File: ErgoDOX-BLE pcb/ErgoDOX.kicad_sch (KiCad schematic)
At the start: 98 parts, among them J1 Conn_01x04, J2 Conn_01x02_Female, J3 Conn_01x02_Female, J4 Conn_01x02, J5 Conn_01x02, P1 USB_C_Plug_USB2.0, Q1 Q_NPN_BCE, SW0:10 SW0:3, SW0:11 SW0:2, SW0:12 SW0:1, SW0:7 SW0:6, SW0:8 SW0:5, SW0:9 SW0:4, SW1:10 SW1:3, SW1:11 SW1:2, SW1:12 SW1:1, SW1:13 SW1:0, SW1:9 SW1:4, SW2:10 SW2:3, SW2:11 SW2:2, SW2:12 SW2:1, SW2:13 SW2:0, SW2:7 SW2:6, SW2:8 SW2:5, SW2:9 SW2:4, SW3:10 SW3:3, SW3:11 SW3:2, SW3:12 SW3:1, SW3:13 SW3:0, SW3:8 SW3:5, SW3:9 SW3:4, SW4:10 SW4:3, SW4:11 SW4:2, SW4:12 SW4:1, SW4:13 SW4:0, SW4:7 SW4:6, SW4:8 SW4:5, SW4:9 SW4:4, SW5:10 SW5:3, SW5:11 SW5:2, SW5:12 SW5:1, SW5:13 SW5:0, SW5:7 SW5:6, SW5:8 SW5:5, SW5:9 SW5:4, U1 MCP23018

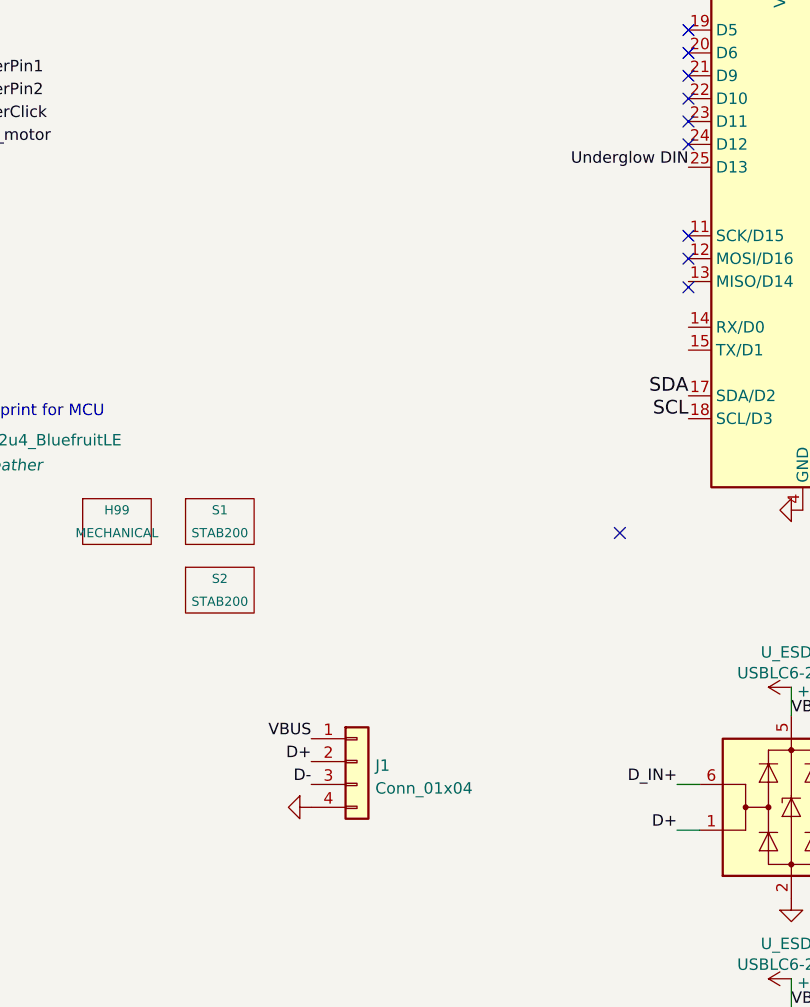
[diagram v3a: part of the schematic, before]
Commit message: Start adding audio port
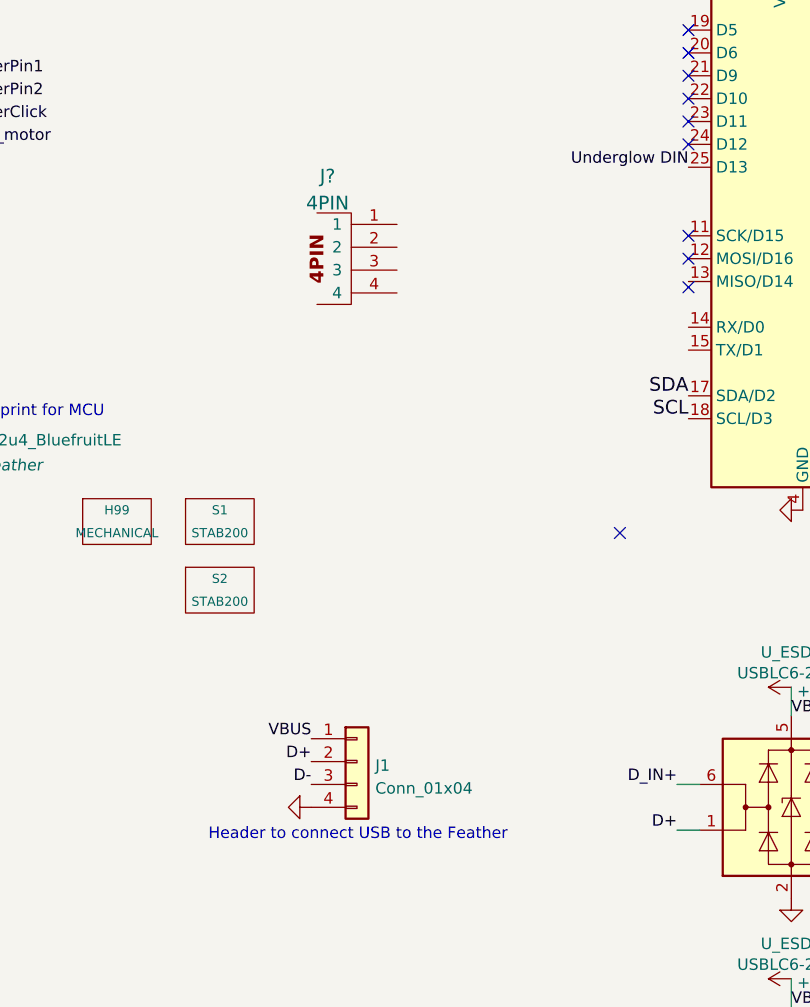
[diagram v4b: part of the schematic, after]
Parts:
- added J?: 4PIN, symbol component:4PIN
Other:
- note added: "Header to connect USB to the Feather"
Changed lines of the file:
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@@
     (effects (font (size 1.27 1.27)) (justify right bottom))
+  )
+  (text "Header to connect USB to the Feather" (at 187.96 148.59 0)
+    (effects (font (size 1.27 1.27)) (justify left bottom))
   )
   (text "Vibration motor circuit. Resistor should be 42 ohms or more"
@@
     )
     (pin "1")
+  )
+  (symbol (lib_id "component:4PIN") (at 203.835 83.82 0) (unit 1)
+    (in_bom yes) (on_board yes) (fields_autoplaced)
+    (property "Reference" "J?" (id 0) (at 201.2023 74.6559 0)
+      (effects (font (size 1.524 1.524)))
+    )
+    (property "Value" "4PIN" (id 1) (at 201.2023 77.6493 0)
+      (effects (font (size 1.524 1.524)))
+    )
+    (property "Footprint" "" (id 2) (at 203.835 83.82 0)
+      (effects (font (size 1.27 1.27)) hide)
+    )
+    (property "Datasheet" "" (id 3) (at 203.835 83.82 0)
+      (effects (font (size 1.27 1.27)) hide)
+    )
+    (pin "1")
+    (pin "2")
+    (pin "3")
+    (pin "4")
   )
   (symbol (lib_id "power:+5V") (at 207.645 216.535 0) (unit 1)
@@
       (reference "J5") (unit 1) (value "Conn_01x02") (footprint "Connector_PinHeader_2.00mm:PinHeader_1x02_P2.00mm_Vertical")
     )
+    (path "/e432a4c5-f3c6-4cf3-aa9d-4b1045904339"
+      (reference "J?") (unit 1) (value "4PIN") (footprint "")
+    )
     (path "/131c2f34-19ec-4ccc-8120-2b0363648606"

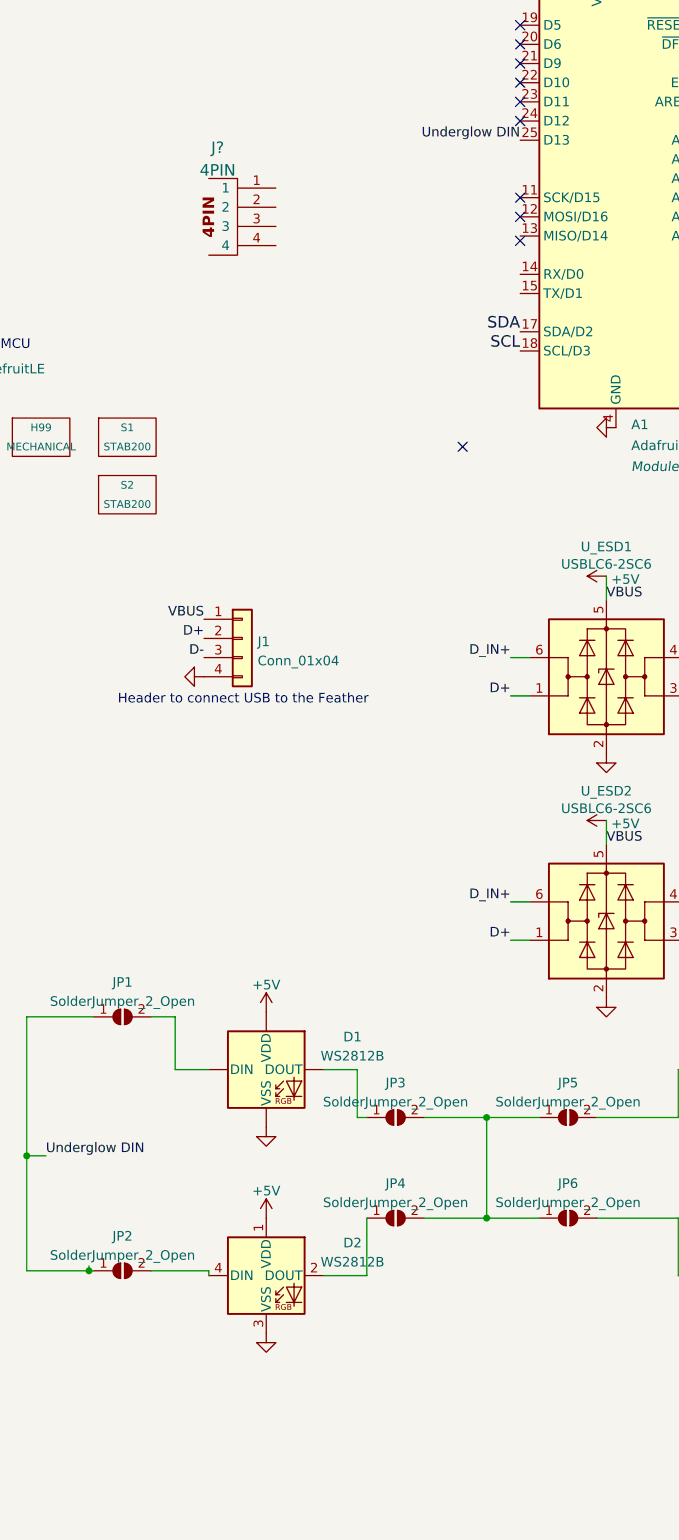
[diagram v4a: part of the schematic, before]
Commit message: Do initial placement of TRRS jack
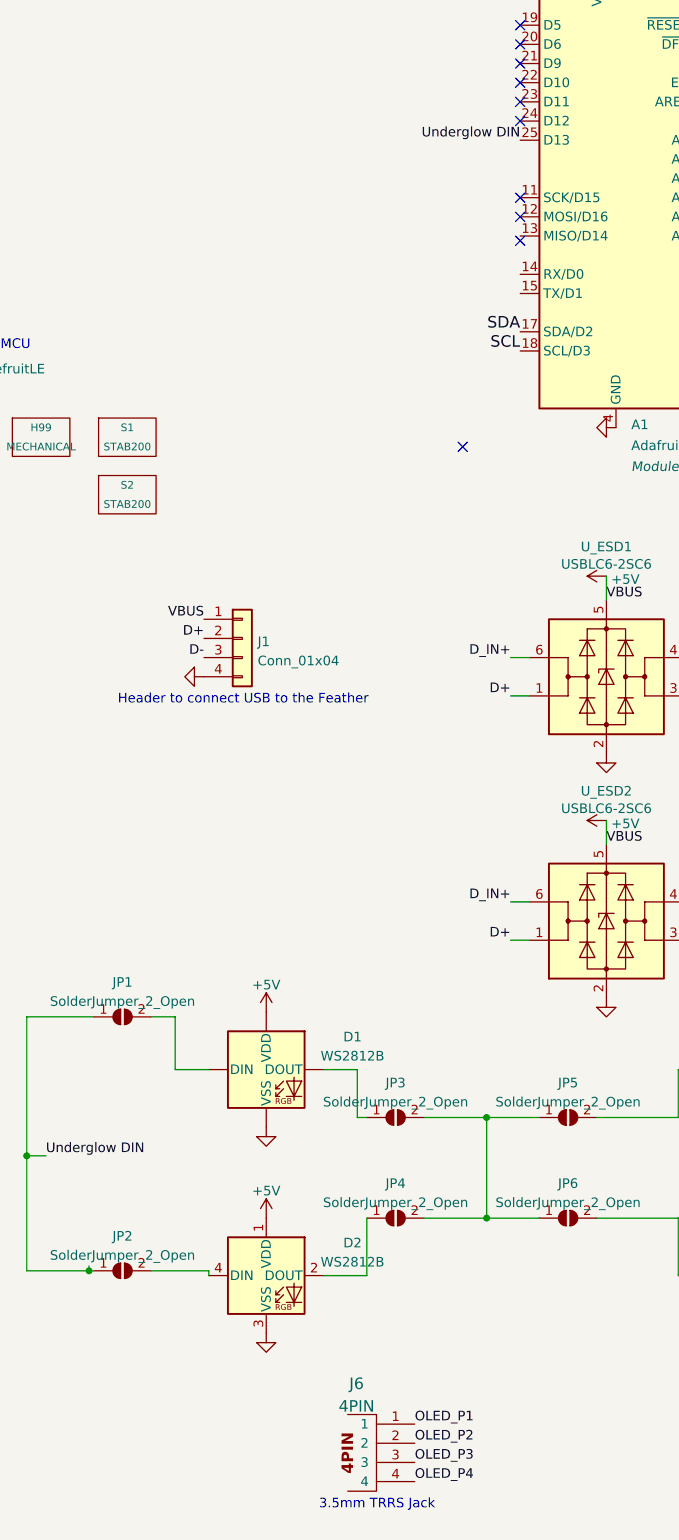
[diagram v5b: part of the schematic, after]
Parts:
- J6: renamed from J?; footprint (none) -> ErgoDOX pcb:4pin35mmAudio
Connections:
- net OLED_P1: now also J6.1
- net OLED_P2: now also J6.2
- net OLED_P3: now also J6.3
- net OLED_P4: now also J6.4
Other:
- note added: "3.5mm TRRS Jack"
- moved on the sheet: J6
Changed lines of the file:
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@@
+    (effects (font (size 1.27 1.27)) (justify left bottom))
+  )
+  (text "3.5mm TRRS Jack" (at 214.63 255.27 0)
     (effects (font (size 1.27 1.27)) (justify left bottom))
   )
@@
     (effects (font (size 1.524 1.524)) (justify left bottom))
   )
+  (label "OLED_P2" (at 227.33 246.38 0)
+    (effects (font (size 1.27 1.27)) (justify left bottom))
+  )
   (label "D+" (at 199.39 139.7 180)
     (effects (font (size 1.27 1.27)) (justify right bottom))
@@
     (effects (font (size 1.27 1.27)) (justify right bottom))
   )
+  (label "OLED_P1" (at 227.33 243.84 0)
+    (effects (font (size 1.27 1.27)) (justify left bottom))
+  )
   (label "ROW3" (at 340.36 85.09 0)
     (effects (font (size 1.524 1.524)) (justify left bottom))
@@
     (effects (font (size 1.524 1.524)) (justify left bottom))
   )
+  (label "OLED_P4" (at 227.33 251.46 0)
+    (effects (font (size 1.27 1.27)) (justify left bottom))
+  )
   (label "VBUS" (at 47.625 80.645 0)
     (effects (font (size 1.27 1.27)) (justify left bottom))
@@
   (label "Reset_SW" (at 58.42 25.4 180)
     (effects (font (size 1.27 1.27)) (justify right bottom))
+  )
+  (label "OLED_P3" (at 227.33 248.92 0)
+    (effects (font (size 1.27 1.27)) (justify left bottom))
   )
   (label "ROW4" (at 340.36 82.55 0)
@@
   (symbol (lib_id "power:+3V3") (at 297.815 188.595 0) (unit 1)
     (in_bom yes) (on_board yes) (fields_autoplaced)
-    (property "Reference" "#PWR?" (id 0) (at 297.815 192.405 0)
+    (property "Reference" "#PWR017" (id 0) (at 297.815 192.405 0)
       (effects (font (size 1.27 1.27)) hide)
     )
@@
     (pin "1")
   )
-  (symbol (lib_id "component:4PIN") (at 203.835 83.82 0) (unit 1)
-    (in_bom yes) (on_board yes) (fields_autoplaced)
-    (property "Reference" "J?" (id 0) (at 201.2023 74.6559 0)
+  (symbol (lib_id "component:4PIN") (at 222.25 247.65 0) (unit 1)
+    (in_bom yes) (on_board yes) (fields_autoplaced)
+    (property "Reference" "J6" (id 0) (at 219.6173 238.4859 0)
       (effects (font (size 1.524 1.524)))
     )
-    (property "Value" "4PIN" (id 1) (at 201.2023 77.6493 0)
+    (property "Value" "4PIN" (id 1) (at 219.6173 241.4793 0)
       (effects (font (size 1.524 1.524)))
     )
-    (property "Footprint" "" (id 2) (at 203.835 83.82 0)
-      (effects (font (size 1.27 1.27)) hide)
-    )
-    (property "Datasheet" "" (id 3) (at 203.835 83.82 0)
+    (property "Footprint" "ErgoDOX pcb:4pin35mmAudio" (id 2) (at 222.25 247.65 0)
+      (effects (font (size 1.27 1.27)) hide)
+    )
+    (property "Datasheet" "" (id 3) (at 222.25 247.65 0)
       (effects (font (size 1.27 1.27)) hide)
     )
@@
       (reference "#PWR016") (unit 1) (value "+5V") (footprint "")
     )
+    (path "/9262c7d3-8469-461f-b560-6292a46b6254"
+      (reference "#PWR017") (unit 1) (value "+3V3") (footprint "")
+    )
     (path "/b2ff08d7-b8f1-4672-b1f1-bb796fc3abc5"
       (reference "#PWR018") (unit 1) (value "GND") (footprint "")
@@
       (reference "#PWR0107") (unit 1) (value "+5V") (footprint "")
     )
-    (path "/9262c7d3-8469-461f-b560-6292a46b6254"
-      (reference "#PWR?") (unit 1) (value "+3V3") (footprint "")
-    )
     (path "/dc3e5149-0691-4e48-82aa-18a33c58d220"
       (reference "A1") (unit 1) (value "Adafruit_Feather_32u4_BluefruitLE") (footprint "Module:Adafruit_Feather")
@@
     )
     (path "/e432a4c5-f3c6-4cf3-aa9d-4b1045904339"
-      (reference "J?") (unit 1) (value "4PIN") (footprint "")
+      (reference "J6") (unit 1) (value "4PIN") (footprint "ErgoDOX pcb:4pin35mmAudio")
     )
     (path "/131c2f34-19ec-4ccc-8120-2b0363648606"

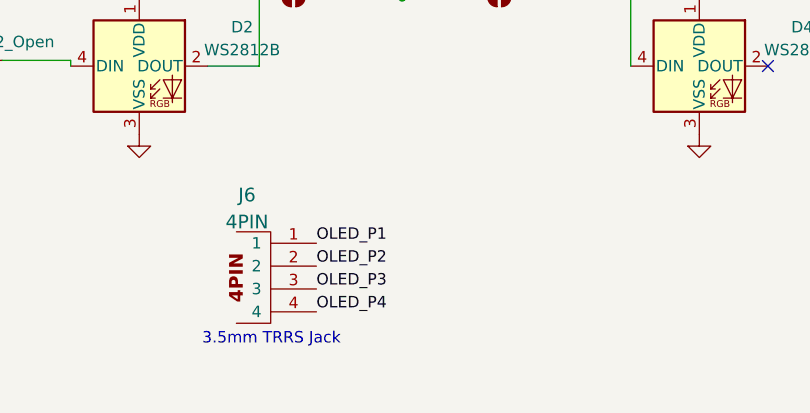
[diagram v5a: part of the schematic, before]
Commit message: Added audio jack and traces
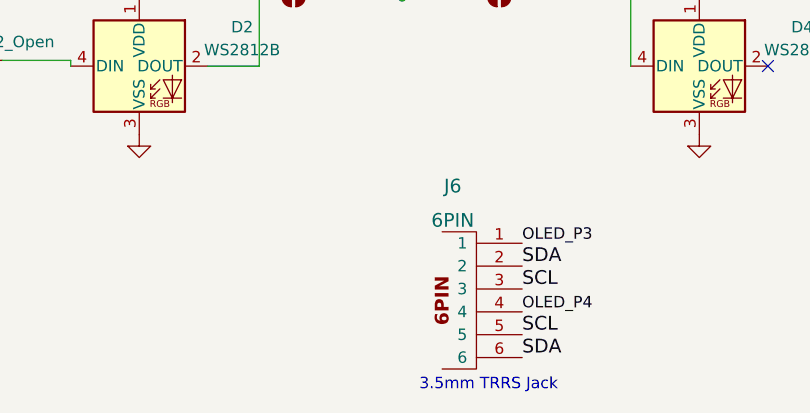
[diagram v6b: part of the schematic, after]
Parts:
- removed J6: 4PIN, ErgoDOX pcb:4pin35mmAudio, symbol component:4PIN
- added J6: 6PIN, ErgoDOX pcb:4pin35mmAudio, symbol component:6PIN
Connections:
- net OLED_P3: now also J6.1
- net OLED_P4: now also J6.4
- net SCL: now also J6.3, J6.5
- net SDA: now also J6.2, J6.6
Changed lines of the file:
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@@
     (effects (font (size 1.27 1.27)) (justify left bottom))
   )
-  (text "3.5mm TRRS Jack" (at 214.63 255.27 0)
+  (text "3.5mm TRRS Jack" (at 238.76 260.35 0)
     (effects (font (size 1.27 1.27)) (justify left bottom))
   )
@@
     (effects (font (size 1.524 1.524)) (justify left bottom))
   )
-  (label "OLED_P2" (at 227.33 246.38 0)
-    (effects (font (size 1.27 1.27)) (justify left bottom))
-  )
   (label "D+" (at 199.39 139.7 180)
     (effects (font (size 1.27 1.27)) (justify right bottom))
@@
     (effects (font (size 1.27 1.27)) (justify left bottom))
   )
+  (label "OLED_P3" (at 250.19 243.84 0)
+    (effects (font (size 1.27 1.27)) (justify left bottom))
+  )
   (label "VBUS" (at 252.73 134.62 0)
     (effects (font (size 1.27 1.27)) (justify left bottom))
@@
     (effects (font (size 1.524 1.524)) (justify right bottom))
   )
+  (label "SDA" (at 250.19 246.38 0)
+    (effects (font (size 1.524 1.524)) (justify left bottom))
+  )
   (label "ROW1" (at 340.36 90.17 0)
     (effects (font (size 1.524 1.524)) (justify left bottom))
@@
     (effects (font (size 1.524 1.524)) (justify left bottom))
   )
+  (label "SDA" (at 250.19 256.54 0)
+    (effects (font (size 1.524 1.524)) (justify left bottom))
+  )
   (label "D+" (at 240.03 179.705 180)
     (effects (font (size 1.27 1.27)) (justify right bottom))
@@
     (effects (font (size 1.27 1.27)) (justify right bottom))
   )
-  (label "OLED_P1" (at 227.33 243.84 0)
+  (label "OLED_P4" (at 250.19 251.46 0)
     (effects (font (size 1.27 1.27)) (justify left bottom))
   )
@@
     (effects (font (size 1.524 1.524)) (justify right bottom))
   )
+  (label "SCL" (at 250.19 254 0)
+    (effects (font (size 1.524 1.524)) (justify left bottom))
+  )
   (label "SCL" (at 336.55 238.125 0)
     (effects (font (size 1.524 1.524)) (justify left bottom))
@@
   (label "OLED_P2" (at 315.595 216.535 180)
     (effects (font (size 1.27 1.27)) (justify right bottom))
+  )
+  (label "SCL" (at 250.19 248.92 0)
+    (effects (font (size 1.524 1.524)) (justify left bottom))
   )
   (label "ROW4" (at 33.02 163.83 180)
@@
     (effects (font (size 1.524 1.524)) (justify left bottom))
   )
-  (label "OLED_P4" (at 227.33 251.46 0)
-    (effects (font (size 1.27 1.27)) (justify left bottom))
-  )
   (label "VBUS" (at 47.625 80.645 0)
     (effects (font (size 1.27 1.27)) (justify left bottom))
@@
   (label "Reset_SW" (at 58.42 25.4 180)
     (effects (font (size 1.27 1.27)) (justify right bottom))
-  )
-  (label "OLED_P3" (at 227.33 248.92 0)
-    (effects (font (size 1.27 1.27)) (justify left bottom))
   )
   (label "ROW4" (at 340.36 82.55 0)
@@
     (pin "2")
   )
+  (symbol (lib_id "component:6PIN") (at 245.11 250.19 0) (unit 1)
+    (in_bom yes) (on_board yes) (fields_autoplaced)
+    (property "Reference" "J6" (id 0) (at 242.4773 237.49 0)
+      (effects (font (size 1.524 1.524)))
+    )
+    (property "Value" "6PIN" (id 1) (at 242.4773 241.3 0)
+      (effects (font (size 1.524 1.524)))
+    )
+    (property "Footprint" "ErgoDOX pcb:4pin35mmAudio" (id 2) (at 245.11 250.19 0)
+      (effects (font (size 1.27 1.27)) hide)
+    )
+    (property "Datasheet" "" (id 3) (at 245.11 250.19 0)
+      (effects (font (size 1.27 1.27)) hide)
+    )
+    (pin "1")
+    (pin "2")
+    (pin "3")
+    (pin "4")
+    (pin "5")
+    (pin "6")
+  )
   (symbol (lib_id "Connector_Generic:Conn_01x02") (at 347.98 190.5 0) (unit 1)
     (in_bom yes) (on_board yes) (fields_autoplaced)
@@
     )
     (pin "1")
-  )
-  (symbol (lib_id "component:4PIN") (at 222.25 247.65 0) (unit 1)
-    (in_bom yes) (on_board yes) (fields_autoplaced)
-    (property "Reference" "J6" (id 0) (at 219.6173 238.4859 0)
-      (effects (font (size 1.524 1.524)))
-    )
-    (property "Value" "4PIN" (id 1) (at 219.6173 241.4793 0)
-      (effects (font (size 1.524 1.524)))
-    )
-    (property "Footprint" "ErgoDOX pcb:4pin35mmAudio" (id 2) (at 222.25 247.65 0)
-      (effects (font (size 1.27 1.27)) hide)
-    )
-    (property "Datasheet" "" (id 3) (at 222.25 247.65 0)
-      (effects (font (size 1.27 1.27)) hide)
-    )
-    (pin "1")
-    (pin "2")
-    (pin "3")
-    (pin "4")
   )
   (symbol (lib_id "power:+5V") (at 207.645 216.535 0) (unit 1)
@@
       (reference "J5") (unit 1) (value "Conn_01x02") (footprint "Connector_PinHeader_2.00mm:PinHeader_1x02_P2.00mm_Vertical")
     )
-    (path "/e432a4c5-f3c6-4cf3-aa9d-4b1045904339"
-      (reference "J6") (unit 1) (value "4PIN") (footprint "ErgoDOX pcb:4pin35mmAudio")
+    (path "/bea7f2ce-f656-49f6-aed6-635d4b2b3bb7"
+      (reference "J6") (unit 1) (value "6PIN") (footprint "ErgoDOX pcb:4pin35mmAudio")
     )
     (path "/131c2f34-19ec-4ccc-8120-2b0363648606"
